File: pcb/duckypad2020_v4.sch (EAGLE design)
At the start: 94 parts, among them IC1 STM32F072C8T6, IC2 REG1117, IC3 74AHCT1G08DBV, SW1 324_SW324_SWITCH_FOOT_HOLE, SW10 KAILH_SWITCH_SOCKET_KAILH_SWI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, SW11 KAILH_SWITCH_SOCKET_KAILH_SWI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, SW12 KAILH_SWITCH_SOCKET_KAILH_SWI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, SW13 KAILH_SWITCH_SOCKET_KAILH_SWI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, SW14 KAILH_SWITCH_SOCKET_KAILH_SWI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, SW15 KAILH_SWITCH_SOCKET_KAILH_SWI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

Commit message: adding components
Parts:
- added R10, R6: 5.1K, joyAnalog:RESISTOR0805-RES
- added SH1: SH10P, duckypad:SH10P
- added U3: USBC_16P, my_usbc_16p:USBC_16P
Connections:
- new net +5V: C29.2, IC2.VIN, SH1.1, U2.VBUS
- new net N$36: R10.1, U3.CC1
- net +3V3: now also SH1.3
- net GND: now also R10.2, R6.2, SH1.11, SH1.12, SH1.2, U3.GND
- net N$1: now also R6.1, U3.CC2; no longer C29.2, IC2.VIN, U2.VBUS
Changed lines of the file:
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@@
 <part name="SW21" library="duckypad" deviceset="SPST_TACT" device="-EVQQ2"/>
 <part name="U$14" library="adafruit_changed" deviceset="PINHD1X2" device=""/>
+<part name="SH1" library="duckypad" deviceset="SH10P" device=""/>
+<part name="+3V39" library="supply1" library_urn="urn:adsk.eagle:library:371" deviceset="+3V3" device=""/>
+<part name="GND64" library="supply1" deviceset="GND" device=""/>
+<part name="GND5" library="supply1" deviceset="GND" device=""/>
+<part name="P+1" library="supply1" library_urn="urn:adsk.eagle:library:371" deviceset="+5V" device=""/>
+<part name="P+2" library="supply1" library_urn="urn:adsk.eagle:library:371" deviceset="+5V" device=""/>
+<part name="U3" library="my_usbc_16p" deviceset="USBC_16P" device=""/>
+<part name="GND8" library="supply1" deviceset="GND" device=""/>
+<part name="R6" library="joyAnalog" deviceset="RESISTOR" device="0805-RES" value="5.1K"/>
+<part name="R10" library="joyAnalog" deviceset="RESISTOR" device="0805-RES" value="5.1K"/>
 </parts>
 <sheets>
@@
 <attribute name="NAME" x="257.81" y="-215.265" size="1.778" layer="95"/>
 <attribute name="VALUE" x="257.81" y="-226.06" size="1.778" layer="96"/>
+</instance>
+<instance part="SH1" gate="G$1" x="388.62" y="-256.54" smashed="yes"/>
+<instance part="+3V39" gate="G$1" x="408.94" y="-246.38" smashed="yes" rot="MR0">
+<attribute name="VALUE" x="411.48" y="-251.46" size="1.778" layer="96" rot="MR90"/>
+</instance>
+<instance part="GND64" gate="1" x="381" y="-276.86" smashed="yes" rot="MR0">
+<attribute name="VALUE" x="383.54" y="-279.4" size="1.778" layer="96" rot="MR0"/>
+</instance>
+<instance part="GND5" gate="1" x="373.38" y="-248.92" smashed="yes" rot="MR0">
+<attribute name="VALUE" x="375.92" y="-251.46" size="1.778" layer="96" rot="MR0"/>
+</instance>
+<instance part="P+1" gate="1" x="78.74" y="-134.62" smashed="yes">
+<attribute name="VALUE" x="76.2" y="-139.7" size="1.778" layer="96" rot="R90"/>
+</instance>
+<instance part="P+2" gate="1" x="373.38" y="-238.76" smashed="yes">
+<attribute name="VALUE" x="370.84" y="-243.84" size="1.778" layer="96" rot="R90"/>
+</instance>
+<instance part="U3" gate="G$1" x="408.94" y="-322.58" smashed="yes" rot="MR0"/>
+<instance part="GND8" gate="1" x="370.84" y="-330.2" smashed="yes" rot="MR0">
+<attribute name="VALUE" x="373.38" y="-332.74" size="1.778" layer="96" rot="MR0"/>
+</instance>
+<instance part="R6" gate="G$1" x="375.92" y="-312.42" smashed="yes" rot="MR0">
+<attribute name="NAME" x="379.73" y="-310.9214" size="1.778" layer="95" rot="MR0"/>
+<attribute name="VALUE" x="379.73" y="-315.722" size="1.778" layer="96" rot="MR0"/>
+<attribute name="NAME" x="379.73" y="-310.9214" size="1.778" layer="95" rot="MR0"/>
+<attribute name="VALUE" x="379.73" y="-315.722" size="1.778" layer="96" rot="MR0"/>
+</instance>
+<instance part="R10" gate="G$1" x="375.92" y="-307.34" smashed="yes" rot="MR0">
+<attribute name="NAME" x="379.73" y="-305.8414" size="1.778" layer="95" rot="MR0"/>
+<attribute name="VALUE" x="379.73" y="-310.642" size="1.778" layer="96" rot="MR0"/>
+<attribute name="NAME" x="379.73" y="-305.8414" size="1.778" layer="95" rot="MR0"/>
+<attribute name="VALUE" x="379.73" y="-310.642" size="1.778" layer="96" rot="MR0"/>
 </instance>
 </instances>
@@
 <pinref part="GND16" gate="1" pin="GND"/>
 </segment>
+<segment>
+<pinref part="SH1" gate="G$1" pin="12"/>
+<pinref part="GND64" gate="1" pin="GND"/>
+<wire x1="386.08" y1="-274.32" x2="381" y2="-274.32" width="0.1524" layer="91"/>
+<pinref part="SH1" gate="G$1" pin="11"/>
+<wire x1="386.08" y1="-271.78" x2="381" y2="-271.78" width="0.1524" layer="91"/>
+<wire x1="381" y1="-271.78" x2="381" y2="-274.32" width="0.1524" layer="91"/>
+<junction x="381" y="-274.32"/>
+</segment>
+<segment>
+<pinref part="SH1" gate="G$1" pin="2"/>
+<pinref part="GND5" gate="1" pin="GND"/>
+<wire x1="386.08" y1="-246.38" x2="373.38" y2="-246.38" width="0.1524" layer="91"/>
+</segment>
+<segment>
+<pinref part="GND8" gate="1" pin="GND"/>
+<wire x1="370.84" y1="-317.5" x2="370.84" y2="-322.58" width="0.1524" layer="91"/>
+<pinref part="R6" gate="G$1" pin="2"/>
+<wire x1="370.84" y1="-322.58" x2="370.84" y2="-327.66" width="0.1524" layer="91"/>
+<wire x1="370.84" y1="-312.42" x2="370.84" y2="-317.5" width="0.1524" layer="91"/>
+<junction x="370.84" y="-312.42"/>
+<pinref part="R10" gate="G$1" pin="2"/>
+<wire x1="370.84" y1="-307.34" x2="370.84" y2="-312.42" width="0.1524" layer="91"/>
+<pinref part="U3" gate="G$1" pin="GND"/>
+<wire x1="424.18" y1="-322.58" x2="370.84" y2="-322.58" width="0.1524" layer="91"/>
+<junction x="370.84" y="-322.58"/>
+</segment>
 </net>
 <net name="SCL" class="0">
@@
 <wire x1="-63.5" y1="60.96" x2="-63.5" y2="58.42" width="0.1524" layer="91"/>
 </segment>
+<segment>
+<pinref part="+3V39" gate="G$1" pin="+3V3"/>
+<pinref part="SH1" gate="G$1" pin="3"/>
+<wire x1="408.94" y1="-248.92" x2="386.08" y2="-248.92" width="0.1524" layer="91"/>
+</segment>
 </net>
 <net name="USB_DP" class="0">
@@
 <wire x1="10.16" y1="-149.86" x2="0" y2="-149.86" width="0.1524" layer="91"/>
 <pinref part="U2" gate="G$1" pin="CC1"/>
-</segment>
-</net>
-<net name="N$1" class="0">
-<segment>
-<pinref part="U2" gate="G$1" pin="VBUS"/>
-<pinref part="IC2" gate="G$1" pin="VIN"/>
-<wire x1="43.18" y1="-144.78" x2="78.74" y2="-144.78" width="0.1524" layer="91"/>
-<wire x1="78.74" y1="-144.78" x2="96.52" y2="-144.78" width="0.1524" layer="91"/>
-<pinref part="C29" gate="G$1" pin="2"/>
-<junction x="78.74" y="-144.78"/>
 </segment>
 </net>
@@
 </segment>
 </net>
+<net name="+5V" class="0">
+<segment>
+<pinref part="U2" gate="G$1" pin="VBUS"/>
+<pinref part="IC2" gate="G$1" pin="VIN"/>
+<wire x1="43.18" y1="-144.78" x2="78.74" y2="-144.78" width="0.1524" layer="91"/>
+<wire x1="78.74" y1="-144.78" x2="96.52" y2="-144.78" width="0.1524" layer="91"/>
+<pinref part="C29" gate="G$1" pin="2"/>
+<junction x="78.74" y="-144.78"/>
+<pinref part="P+1" gate="1" pin="+5V"/>
+<wire x1="78.74" y1="-137.16" x2="78.74" y2="-144.78" width="0.1524" layer="91"/>
+</segment>
+<segment>
+<pinref part="SH1" gate="G$1" pin="1"/>
+<pinref part="P+2" gate="1" pin="+5V"/>
+<wire x1="386.08" y1="-243.84" x2="373.38" y2="-243.84" width="0.1524" layer="91"/>
+<wire x1="373.38" y1="-243.84" x2="373.38" y2="-241.3" width="0.1524" layer="91"/>
+</segment>
+</net>
+<net name="N$1" class="0">
+<segment>
+<pinref part="R6" gate="G$1" pin="1"/>
+<wire x1="383.54" y1="-312.42" x2="381" y2="-312.42" width="0.1524" layer="91"/>
+<wire x1="391.16" y1="-309.88" x2="383.54" y2="-309.88" width="0.1524" layer="91"/>
+<wire x1="383.54" y1="-309.88" x2="383.54" y2="-312.42" width="0.1524" layer="91"/>
+<pinref part="U3" gate="G$1" pin="CC2"/>
+</segment>
+</net>
+<net name="N$36" class="0">
+<segment>
+<pinref part="R10" gate="G$1" pin="1"/>
+<wire x1="391.16" y1="-307.34" x2="381" y2="-307.34" width="0.1524" layer="91"/>
+<pinref part="U3" gate="G$1" pin="CC1"/>
+</segment>
+</net>

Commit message: v4 draft done
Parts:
- removed TP1, TP2, TP3, TP5: PTR1TP11SQ, testpad:PTR1TP11SQ
- removed TP4: PTR1TP09R, testpad:PTR1TP09R
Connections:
- new net N$37: IC1PORTA_L.PA3, SH1.8
- net +3V3: now also SH1.10
- net +5V: now also U3.VBUS
- net BUTTON_DEBUG: no longer IC1PORTA_L.PA3
- net N$13: now also IC1PORTB_L.PB1, SH1.7; no longer IC1PORTB_L.PB2, TP2.TP
- net N$16: now also IC1PORTB_H.PB11, U3.DN1, U3.DN2; no longer IC1PORTB_H.PB10, TP3.TP
- net N$2: now also IC1PORTB_L.PB2, SH1.6; no longer IC1PORTB_L.PB1, TP1.TP
- net N$30: now also IC1PORTB_H.PB10, U3.DP1, U3.DP2; no longer IC1PORTB_H.PB11, TP4.TP
- net N$35: now also SH1.5; no longer TP5.TP

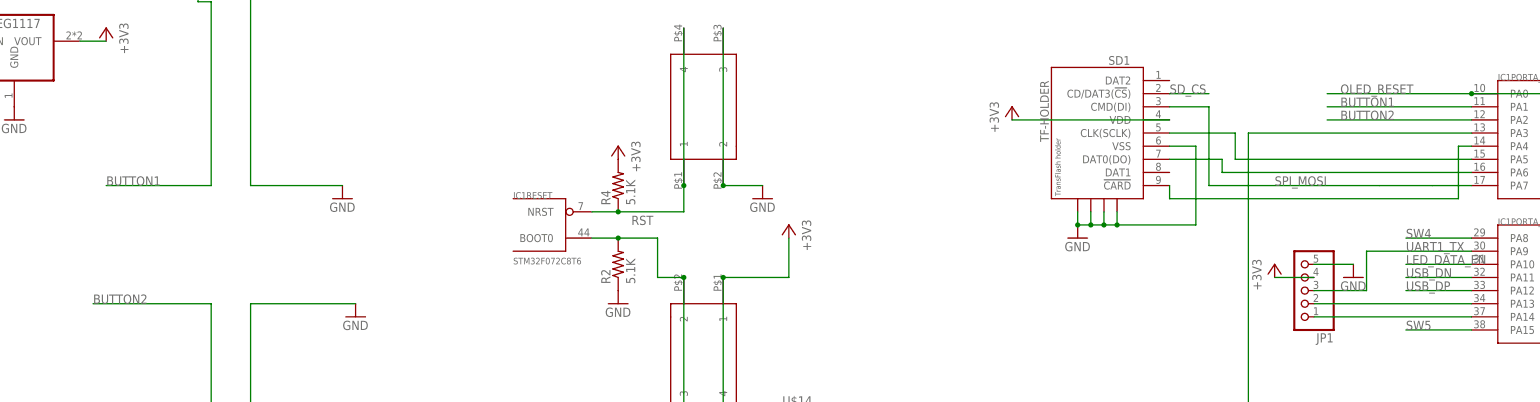
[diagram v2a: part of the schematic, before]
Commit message: adjusted signal names
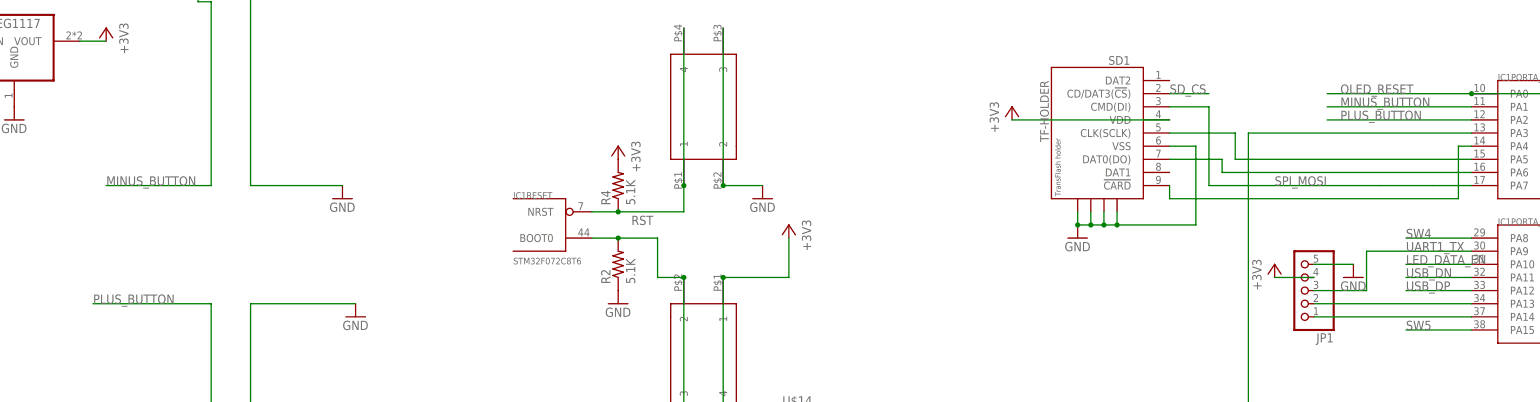
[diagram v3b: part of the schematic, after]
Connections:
- net BUTTON1 renamed MINUS_BUTTON
- net BUTTON2 renamed PLUS_BUTTON
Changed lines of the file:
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@@
 </segment>
 </net>
-<net name="BUTTON1" class="0">
+<net name="MINUS_BUTTON" class="0">
 <segment>
 <label x="127" y="-172.72" size="1.778" layer="95"/>
@@
 </segment>
 </net>
-<net name="BUTTON2" class="0">
+<net name="PLUS_BUTTON" class="0">
 <segment>
 <wire x1="124.46" y1="-195.58" x2="147.32" y2="-195.58" width="0.1524" layer="91"/>
